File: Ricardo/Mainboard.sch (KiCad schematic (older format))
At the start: 82 parts, among them J1 USB_B_Micro, J10 Conn_01x02_Male, J12 Conn_01x02_Male, J2 8P8C_LED, J3 Micro_SD_Card_Det, J9 Conn_01x02_Male, Q1 MMDT2222A, Q3 PMV20ENR, U1 CP2102N-A01-GQFN24, U2 SN65HVD230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

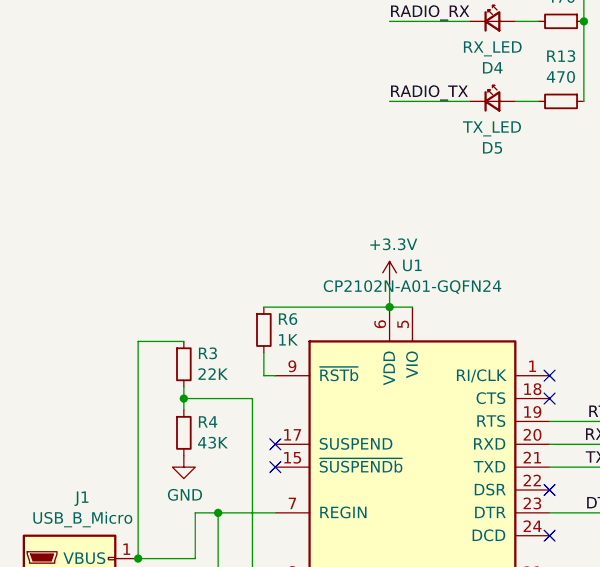
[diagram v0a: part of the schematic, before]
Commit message: RICARDO-V3 added power through usb, fixed issue with power plane on layer3
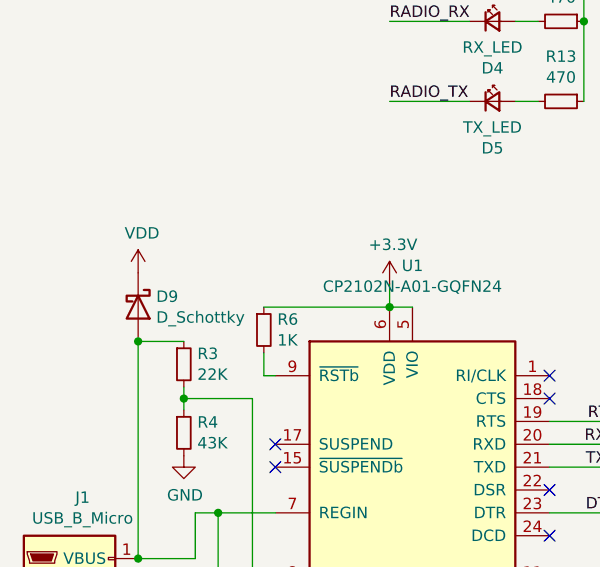
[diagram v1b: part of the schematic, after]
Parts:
- added D9: D_Schottky, Diode_SMD:D_SOD-123F, symbol Device:D_Schottky
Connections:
- net VDD: now also D9.1 (K)
- net at D1.2 (K), J1.1 (VBUS), R3.1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: now also D9.2 (A)
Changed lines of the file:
@@
 	0    1    1    0
 $EndComp
+$Comp
+L Device:D_Schottky D9
+U 1 1 5E667A26
+P 1050 2900
+F 0 "D9" V 1004 2979 50  0000 L CNN
+F 1 "D_Schottky" V 1095 2979 50  0000 L CNN
+F 2 "Diode_SMD:D_SOD-123F" H 1050 2900 50  0001 C CNN
+F 3 "~" H 1050 2900 50  0001 C CNN
+	1    1050 2900
+	0    1    1    0
+$EndComp
+Connection ~ 1050 3050
+$Comp
+L power:VDD #PWR053
+U 1 1 5E668CEC
+P 1050 2750
+F 0 "#PWR053" H 1050 2600 50  0001 C CNN
+F 1 "VDD" H 1067 2923 50  0000 C CNN
+F 2 "" H 1050 2750 50  0001 C CNN
+F 3 "" H 1050 2750 50  0001 C CNN
+	1    1050 2750
+	1    0    0    -1
+$EndComp
 $EndSCHEMATC

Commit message: SANIC Branch
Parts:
- J1: symbol Connector:USB_B_Micro -> Mainboard-rescue:USB_B_Micro-Connector
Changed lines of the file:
@@
 RADIO_TX
 $Comp
-L Connector:USB_B_Micro J1
+L Mainboard-rescue:USB_B_Micro-Connector J1
 U 1 1 5DF84F1A
 P 750 4200
@@
 	1    0    0    -1
 $EndComp
-Connection ~ 1050 4000
-Connection ~ 750  4600
 Wire Wire Line
 	1050 4400 1300 4400

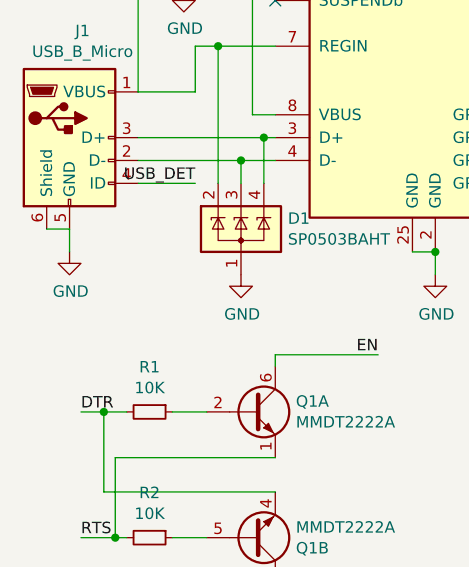
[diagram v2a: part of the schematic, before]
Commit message: updated
sized voltage regulator components
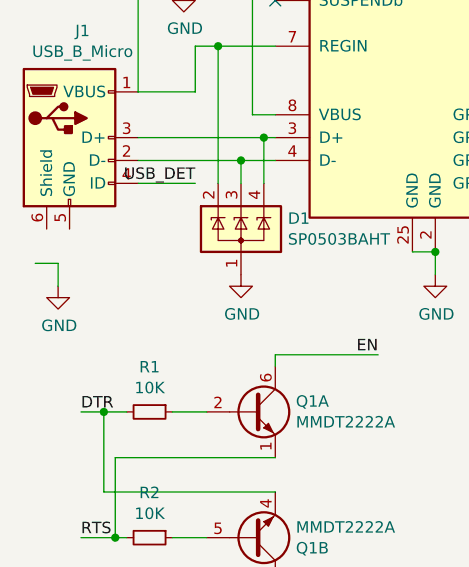
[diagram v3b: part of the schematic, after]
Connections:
- net GND: no longer J1.5 (GND), J1.6 (Shield)
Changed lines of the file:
@@
 L power:GND #PWR01
 U 1 1 5DAD9189
-P 750 4700
-F 0 "#PWR01" H 750 4450 50  0001 C CNN
-F 1 "GND" H 755 4527 50  0000 C CNN
-F 2 "" H 750 4700 50  0001 C CNN
-F 3 "" H 750 4700 50  0001 C CNN
-	1    750  4700
+P 700 4850
+F 0 "#PWR01" H 700 4600 50  0001 C CNN
+F 1 "GND" H 705 4677 50  0000 C CNN
+F 2 "" H 700 4850 50  0001 C CNN
+F 3 "" H 700 4850 50  0001 C CNN
+	1    700  4850
 	1    0    0    -1
 $EndComp
 Wire Wire Line
-	750  4700 750  4600
+	700  4850 700  4750
 Wire Wire Line
-	750  4600 650  4600
+	700  4750 600  4750
 Wire Wire Line
 	1300 4000 1300 3800
